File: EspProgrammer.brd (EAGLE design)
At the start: 31.1 x 17.8 mm, 11 parts

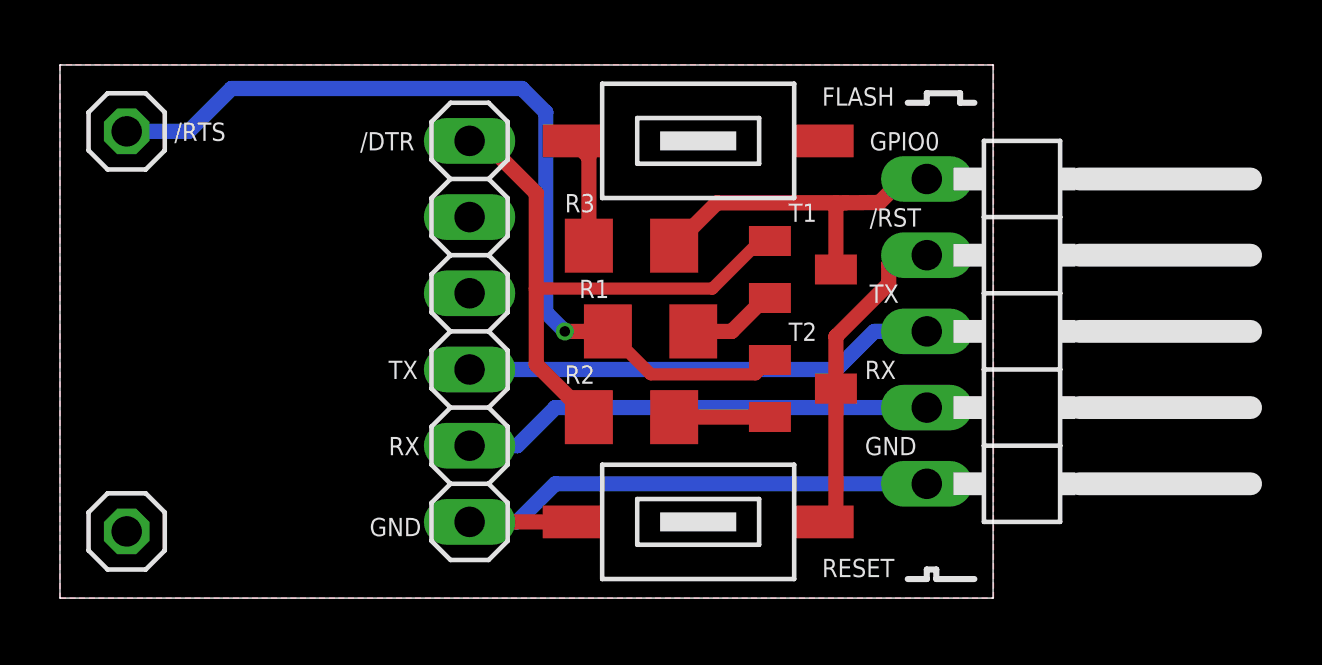
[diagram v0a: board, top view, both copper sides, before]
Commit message: change transistor package
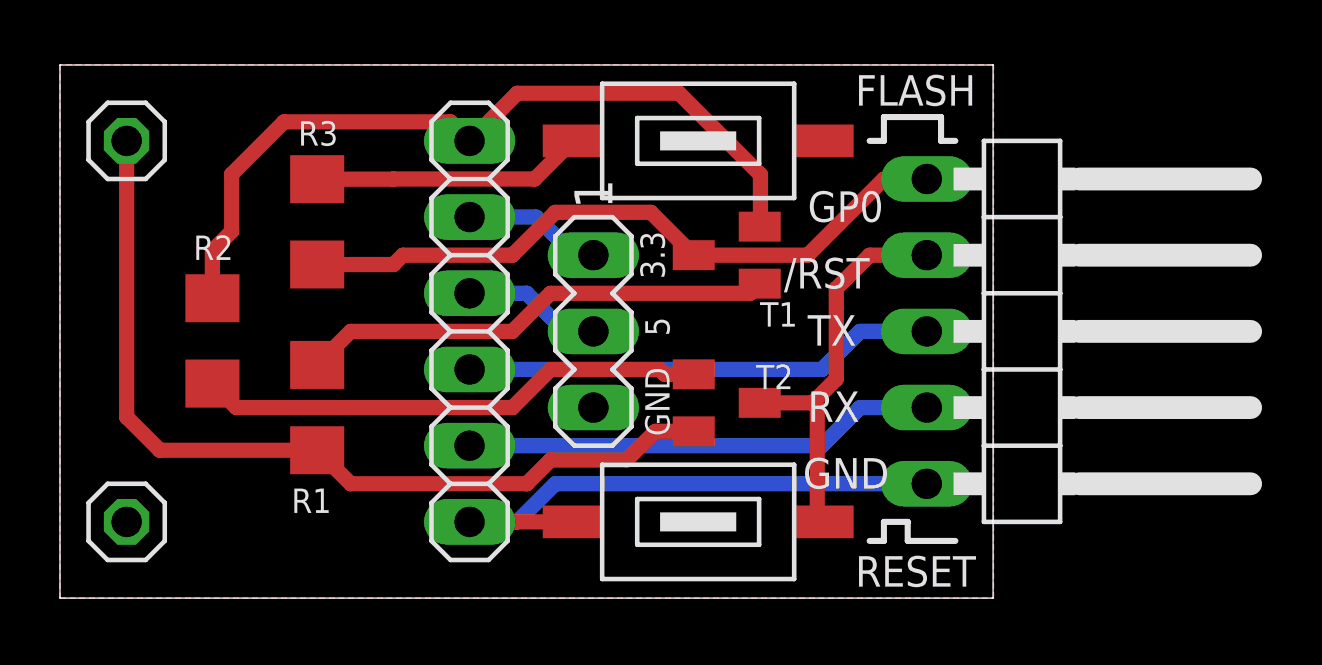
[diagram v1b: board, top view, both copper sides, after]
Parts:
- added SV1: (no value), con-lstb:MA03-1
- R1, R2: value (none) -> 12k
- R3: value (none) -> 470
- T1, T2: value (none) -> BC817-40LT1SMD; device transistor:SOT23-EBC -> transistor-npn:SOT23-BEC
- moved R2 14.2 mm to (5.08, 8.57), turned to 270 degrees
- moved R1 11.4 mm to (8.57, 6.35), turned to 90 degrees
- moved R3 10.5 mm to (8.57, 12.5), turned to 270 degrees
- moved T1 2.58 mm to (22.2, 11.4), turned to 90 degrees
- moved T2 2.58 mm to (22.2, 6.51)
- moved LSP2 0.32 mm to (2.22, 2.54)
- moved LSP3 0.32 mm to (2.22, 15.2)
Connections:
- new net 3V3: JP2.5, SV1.1
- new net 5V: JP2.4, SV1.2
- net GND: now also SV1.3
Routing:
- net N$2: track 3.19 -> 17.0 mm
- net N$1: track 3.02 -> 15.9 mm
- net GPIO0: track 11.6 -> 22.7 mm
- net DTR: track 19.6 -> 26.5 mm
- net N$3: track 3.71 -> 9.05 mm
- net 5V: track 0.00 -> 4.65 mm
- net 3V3: track 0.00 -> 4.65 mm
- net RST: track 10.9 -> 13.5 mm
- net RTS: track 30.1 -> 29.8 mm, vias 1 -> 0
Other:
- board text added: "3.3"
- board text added: "5"
- board text added: "ESP Programmer 12/2020 ThoMo V1.4"
- board text added: "GP0"
- board text removed: "/DTR"
- board text removed: "/RTS"
- board text removed: "ESP Programmer 07/2019 ThoMo V1.0"
